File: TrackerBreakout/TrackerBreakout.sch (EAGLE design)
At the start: 13 parts

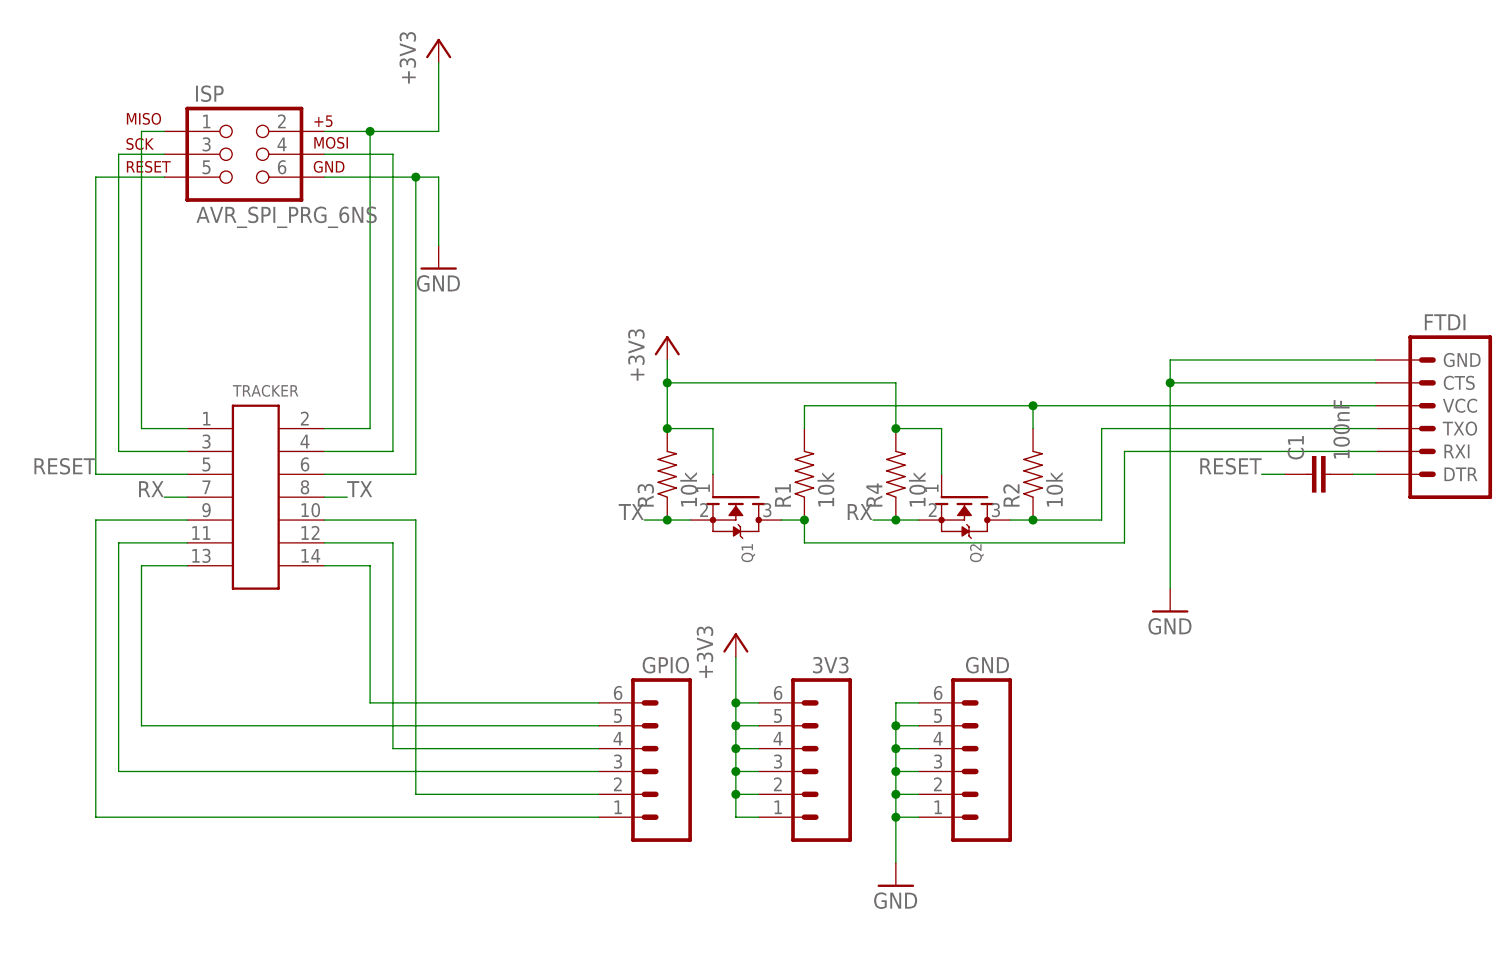
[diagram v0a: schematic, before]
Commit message: fix connector direction
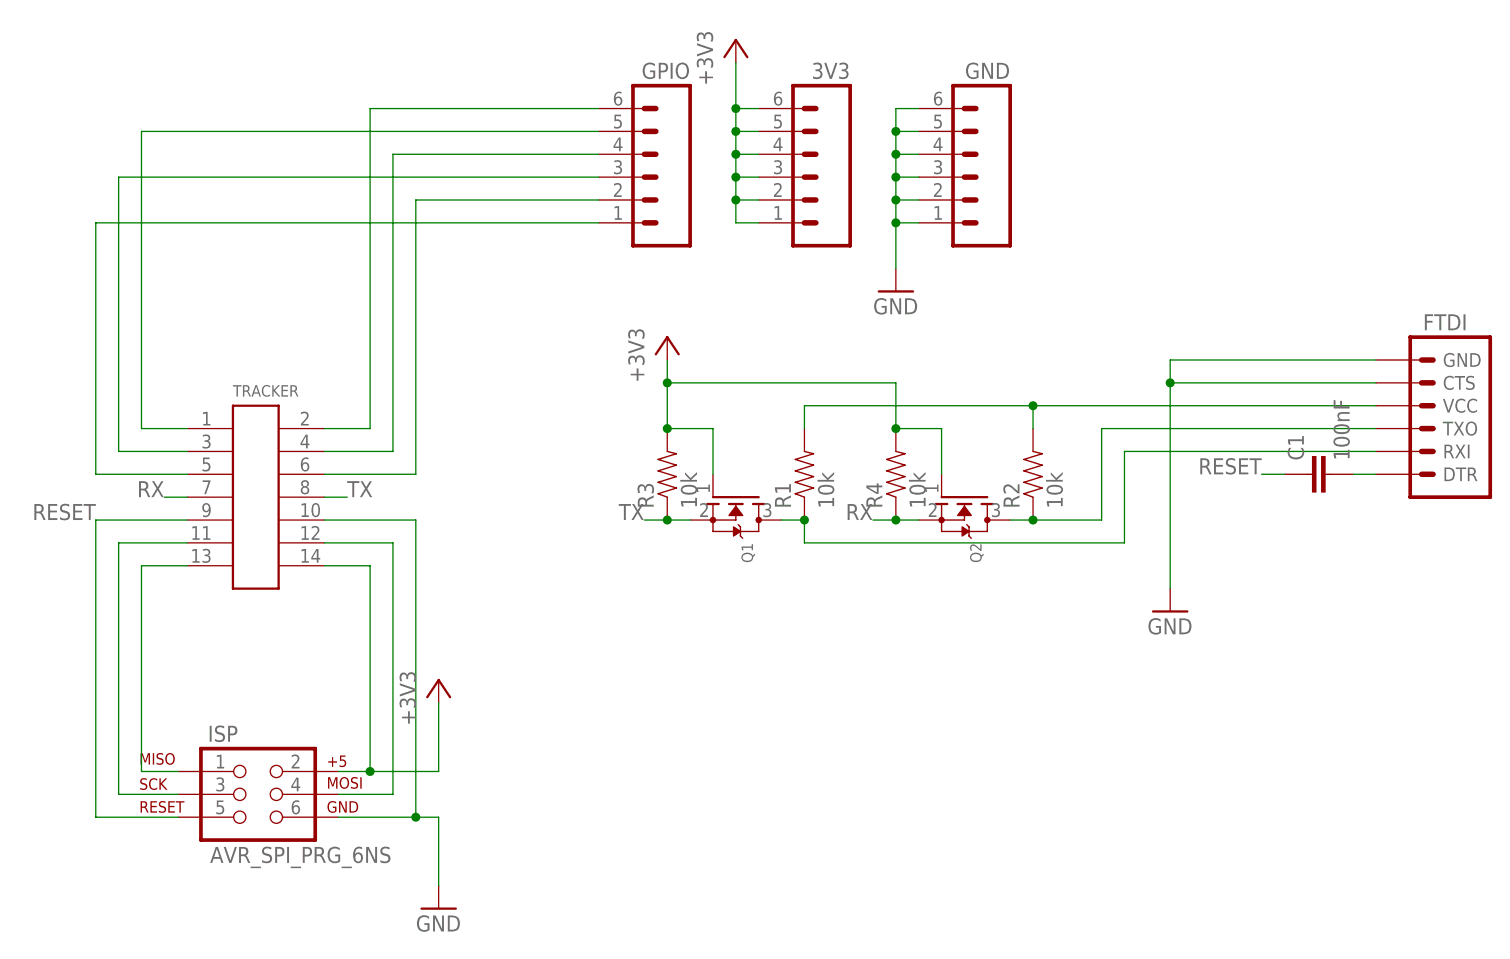
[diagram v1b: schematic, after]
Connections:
- net +3V3: now also TRACKER.14; no longer TRACKER.2
- net GND: now also TRACKER.10; no longer TRACKER.6
- net N$1: now also TRACKER.5; no longer TRACKER.9
- net N$11: now also TRACKER.13; no longer TRACKER.1
- net N$2: now also TRACKER.6; no longer TRACKER.10
- net N$3: now also TRACKER.3; no longer TRACKER.11
- net N$4: now also TRACKER.4; no longer TRACKER.12
- net N$5: now also TRACKER.1; no longer TRACKER.13
- net N$6: now also TRACKER.2; no longer TRACKER.14
- net N$7: now also TRACKER.11; no longer TRACKER.3
- net N$9: now also TRACKER.12; no longer TRACKER.4
- net RESET: now also TRACKER.9; no longer TRACKER.5
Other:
- moved on the sheet: 3V3, GND, GPIO, ISP
